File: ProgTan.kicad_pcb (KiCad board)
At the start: 2 copper layers, 96.5 x 114.3 mm, 10 parts, among them P1 Power, P2 ESP_A, P3 ESP_B, P4 MOTOR2, P5 MOTOR1, P6 Sensor Proximidad, P7 LM7805, U2 L294D

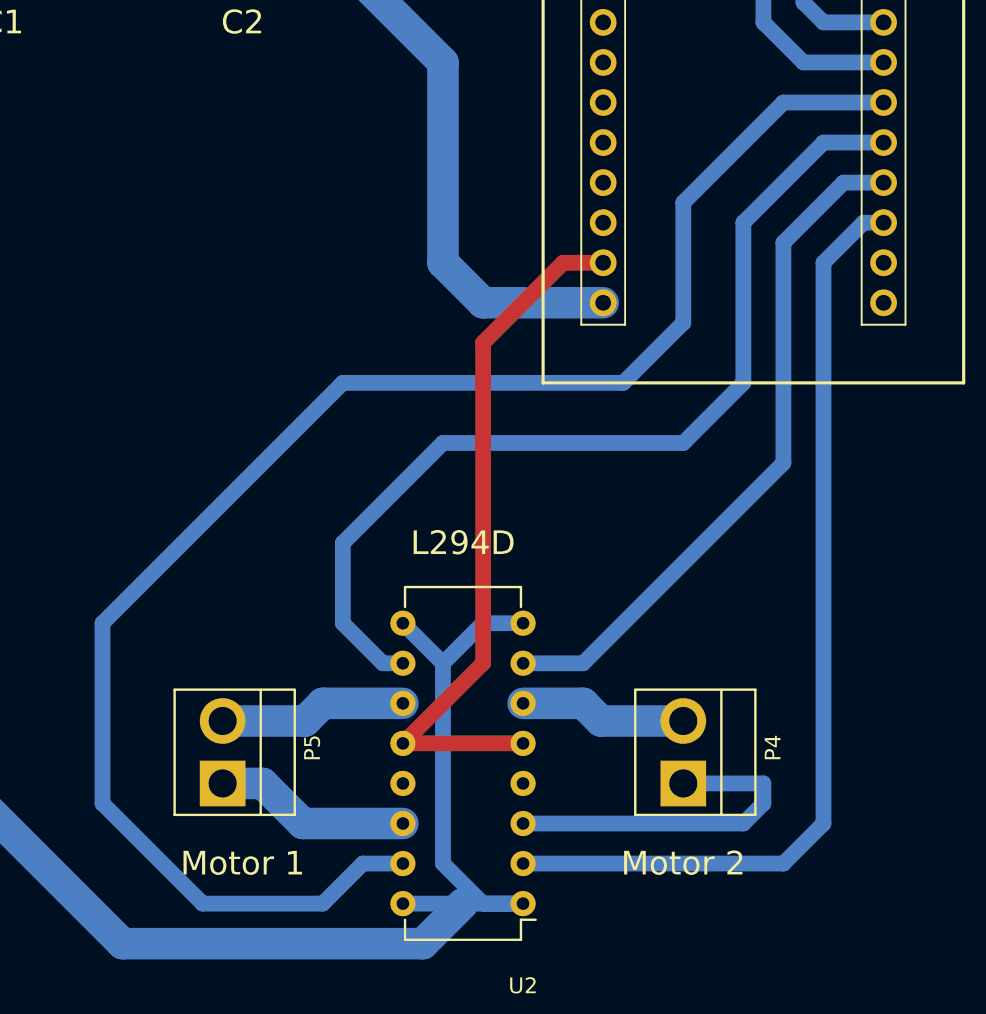
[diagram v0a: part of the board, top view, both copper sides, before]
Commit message: Modificación en las rutas de tierra
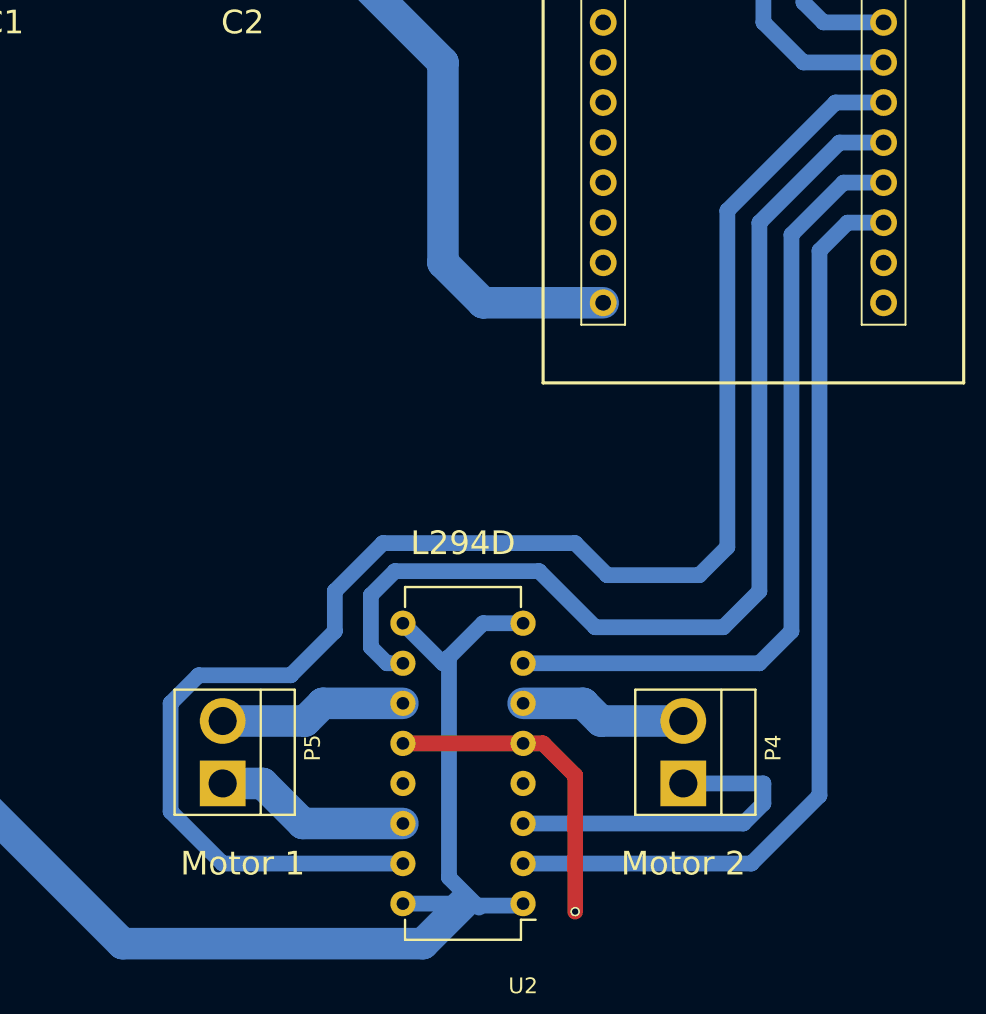
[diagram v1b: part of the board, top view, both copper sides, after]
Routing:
- net GND: track 44.8 -> 20.4 mm, vias 0 -> 1
- net /GPI03: track 43.7 -> 50.2 mm
- net /GPI15: track 60.7 -> 66.8 mm
- net /Vin: track 172.4 -> 169.4 mm
- net /GPI13: track 101.8 -> 99.6 mm
- net /GPI01: track 60.5 -> 59.9 mm

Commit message: General fixes
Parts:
- added LED1: LED, LEDs:LED-3MM, F.Cu at (128.3, 70.5)
- added LED2: LED, LEDs:LED-3MM, F.Cu at (128.9, 61.0)
- added P8: Sensor Infrarrojo, Socket_Strips:Socket_Strip_Straight_1x03, F.Cu at (173.4, 134.6)
- moved P2 4.44 mm to (140.3, 66.0)
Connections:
- P2 pad 2: GND -> (no net)
- P2 pad 3: (no net) -> /GPI10
- P2 pad 4: (no net) -> /GPI09
- P3 pad 12: /GPI03 -> (no net)
- P3 pad 13: /GPI01 -> (no net)
- P3 pad 3: (no net) -> /GPI04
- P3 pad 4: (no net) -> /GPI00
- P3 pad 5: (no net) -> /GPI02
- P6 pad 2: /GPI12 -> /GPI02
- P6 pad 3: /GPI14 -> /GPI00
- U2 pad 2: /GPI01 -> /GPI14
- U2 pad 7: /GPI03 -> /GPI12
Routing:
- net /Vo: track 103.2 -> 213.2 mm
- net /GPI04: track 0.00 -> 68.4 mm
- net /GPI01: track 59.9 -> 0.00 mm
- net /GPI03: track 50.2 -> 0.00 mm
- net /GPI02: track 0.00 -> 48.0 mm
- net /GPI00: track 0.00 -> 44.1 mm
- net /GPI14: track 55.7 -> 79.2 mm
- net /GPI10: track 0.00 -> 14.6 mm
- net /GPI09: track 0.00 -> 10.8 mm
- net /GPI12: track 60.1 -> 62.6 mm
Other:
- board text added: "Jorge Garzon Camilo Vargas Temas Avanzados de Lenguajes de Programación Universidad Nacional de Colombia"
- board text added: "Sensor Infrarrojo"
